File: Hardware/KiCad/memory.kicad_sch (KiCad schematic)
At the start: 12 parts, among them J3 Micro_SD_Card_Det, U2 W25Q16

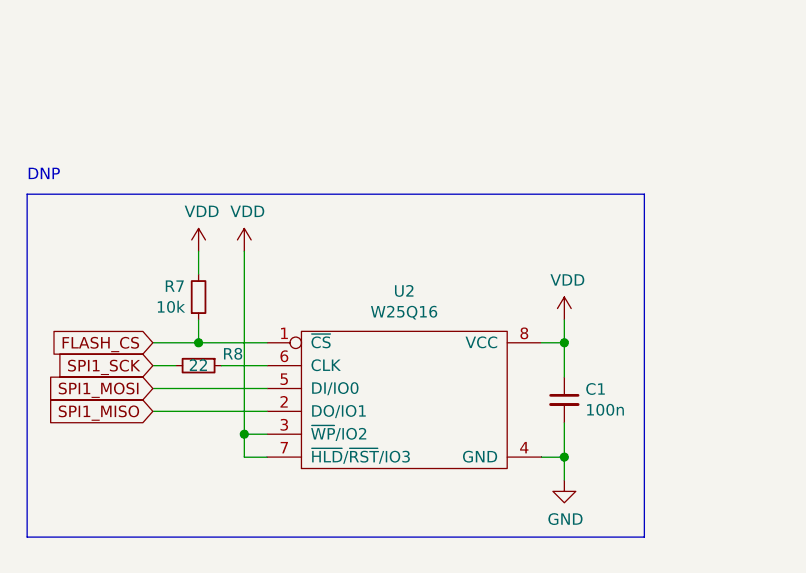
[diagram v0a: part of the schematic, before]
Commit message: fix issue 21 & 20 & move MCU to align w/ grid
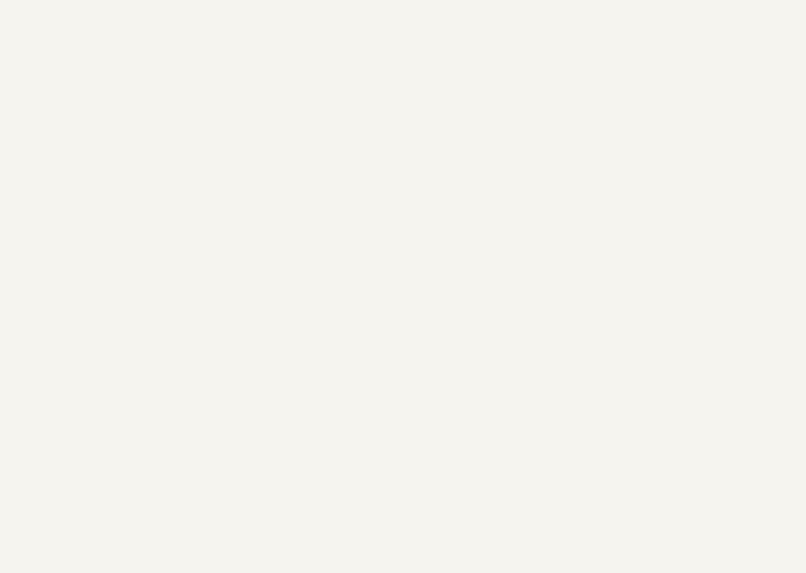
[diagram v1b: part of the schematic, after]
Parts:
- removed C1: 100n, pkl_dipol:C_0603, symbol pkl_device:pkl_C_Small
- removed R7: 10k, pkl_dipol:R_0603, symbol pkl_device:pkl_R_Small
- removed R8: 22, pkl_dipol:R_0603, symbol pkl_device:pkl_R_Small
- removed U2: W25Q16, Package_SO:SOIC-8_3.9x4.9mm_P1.27mm, symbol pkl_memory:W25Q
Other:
- note removed: "DNP"

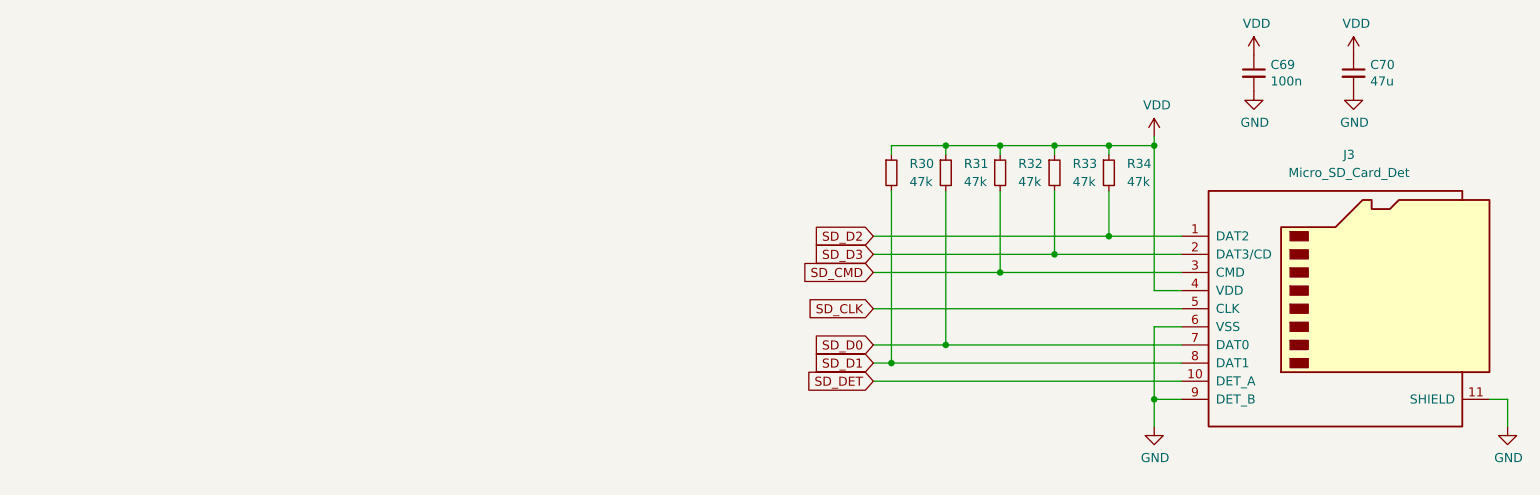
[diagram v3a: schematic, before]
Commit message: Minor corrections
- fixed microphone connection and part values
- added a few TPs
- changed C27 footprint
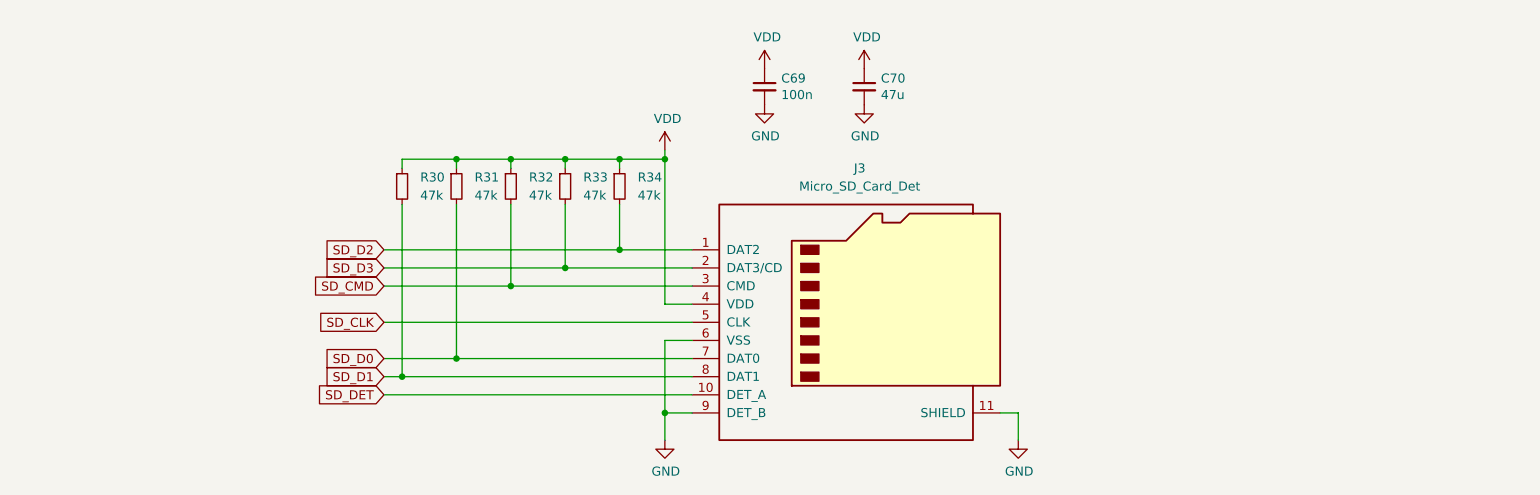
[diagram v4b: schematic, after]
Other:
- moved on the sheet: C69, C70, J3, R30, R31, R32, R33, R34
